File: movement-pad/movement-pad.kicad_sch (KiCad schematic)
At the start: 1 part

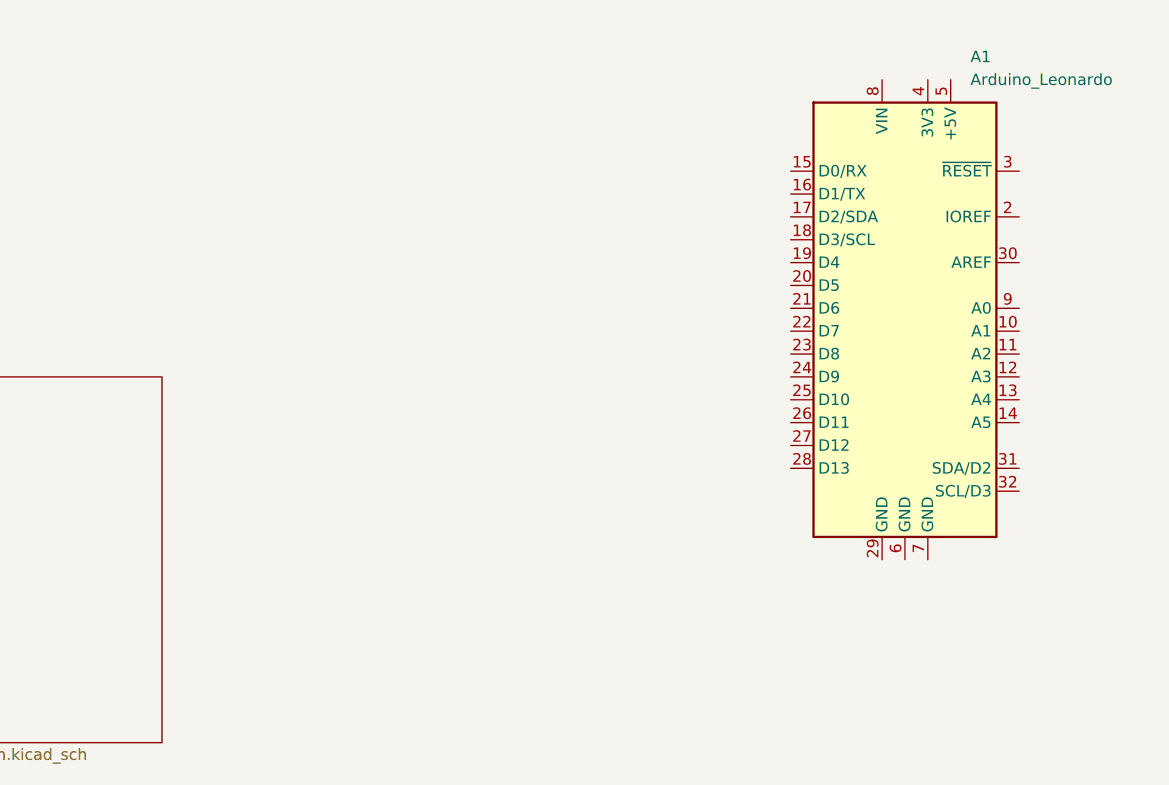
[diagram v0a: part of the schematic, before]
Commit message: worked on schematic in lecture
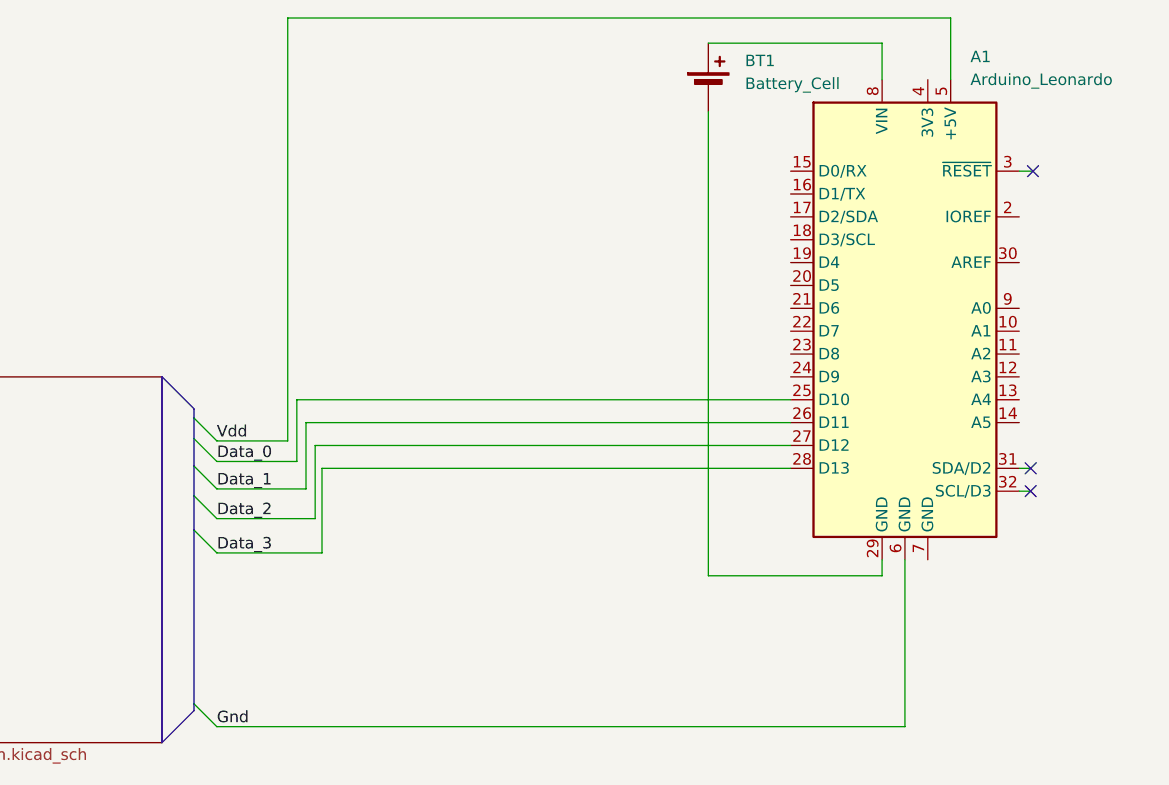
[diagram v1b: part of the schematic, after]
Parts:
- added BT1: Battery_Cell, symbol Device:Battery_Cell
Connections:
- net Data_0: now reaches A1.25 (D10)
- net Data_1: now reaches A1.26 (D11)
- net Data_2: now reaches A1.27 (D12)
- net Data_3: now reaches A1.28 (D13)
- net at A1.29 (GND): now also BT1.2 (-)
- net Vdd: now reaches A1.5 (+5V)
- net Gnd: now reaches A1.6 (GND)
- net at A1.8 (VIN): now also BT1.1 (+)
- no-connect marks 0 -> 3

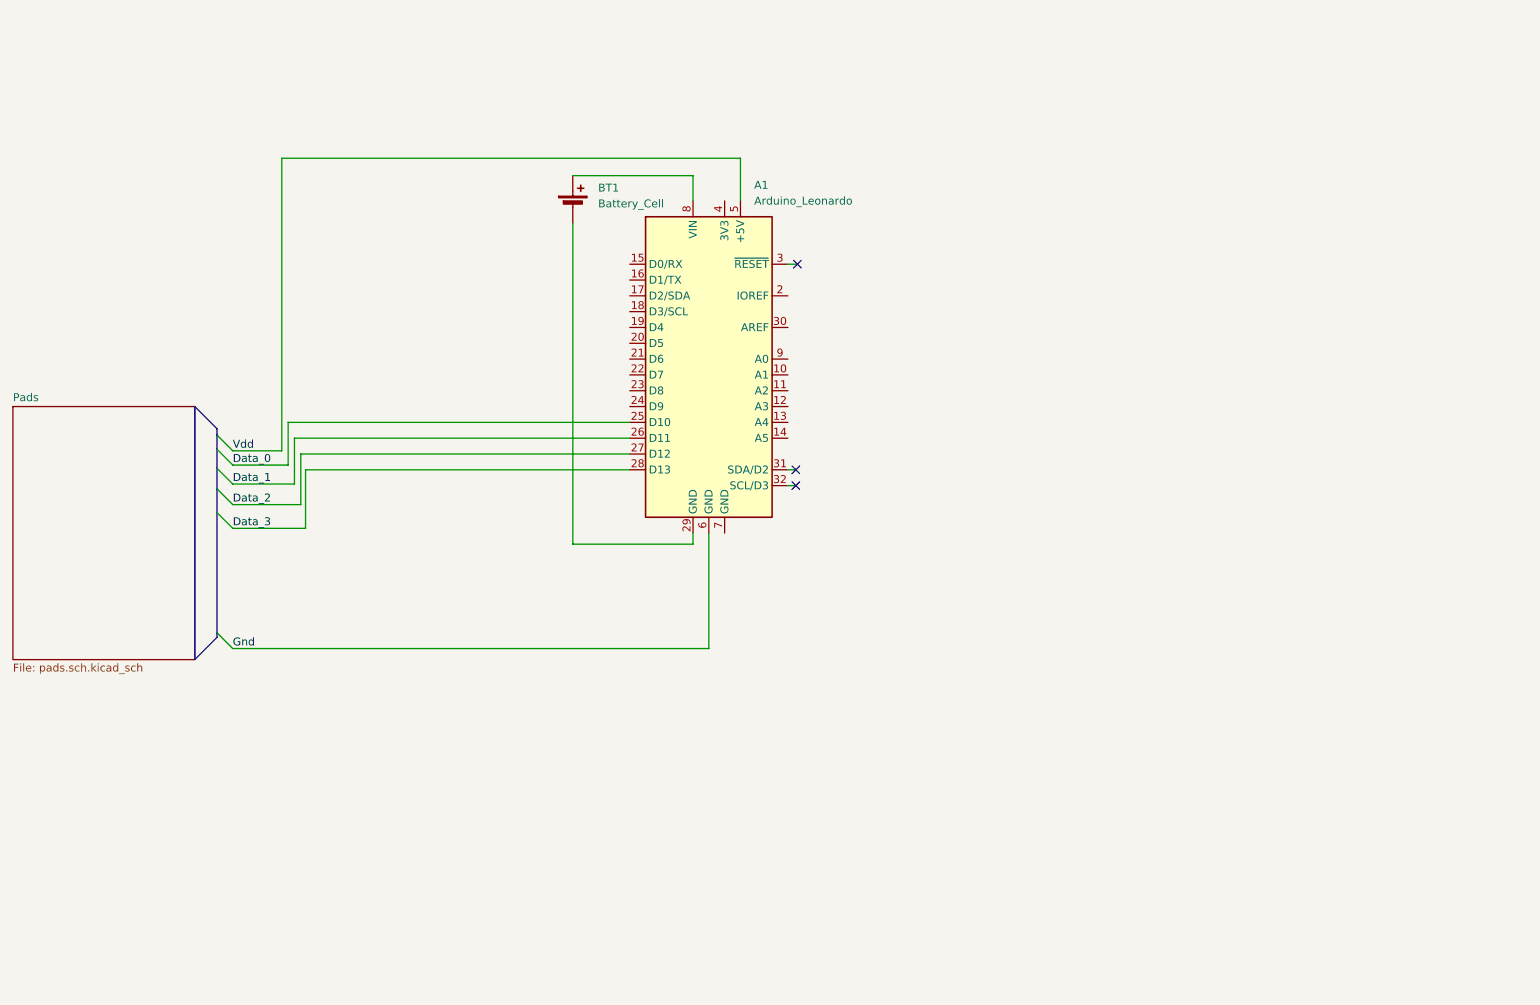
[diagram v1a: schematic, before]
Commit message: updated movement pad
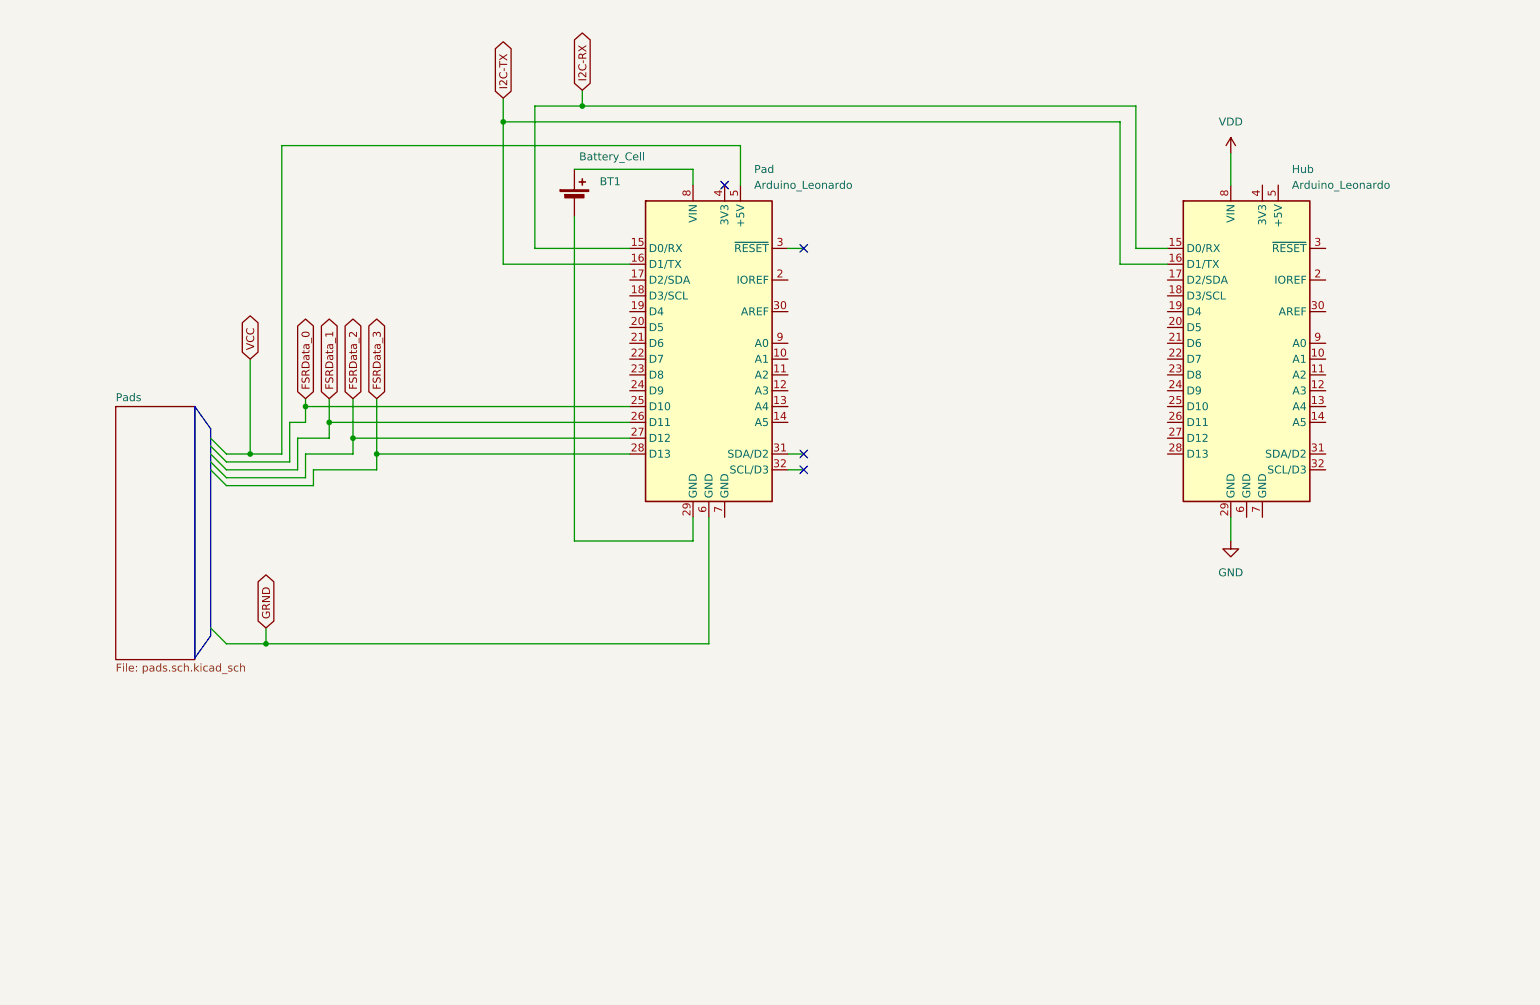
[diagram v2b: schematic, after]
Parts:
- added Hub: Arduino_Leonardo, Module:Arduino_UNO_R3, symbol MCU_Module:Arduino_Leonardo
- renumbered A1 to Pad
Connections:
- net I2C-RX: now reaches Pad.15 (D0/RX)
- net I2C-RX: now also Hub.15 (D0/RX)
- net I2C-TX: now reaches Pad.16 (D1/TX)
- net I2C-TX: now also Hub.16 (D1/TX)
- net Data_0 renamed FSRData_0
- net Data_1 renamed FSRData_1
- net Data_2 renamed FSRData_2
- net Data_3 renamed FSRData_3
- net Gnd renamed GRND
- net Vdd renamed VCC
- new net GND: Hub.29 (GND)
- new net VDD: Hub.8 (VIN)
- no-connect marks 3 -> 4
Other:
- moved on the sheet: BT1, Pad

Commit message: tinkered with top level pad, add in i2c chip?
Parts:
- removed Hub: Arduino_Leonardo, Module:Arduino_UNO_R3, symbol MCU_Module:Arduino_Leonardo
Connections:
- net I2C-RX: no longer names the net of Pad.15 (D0/RX)
- net I2C-TX: no longer names the net of Pad.16 (D1/TX)

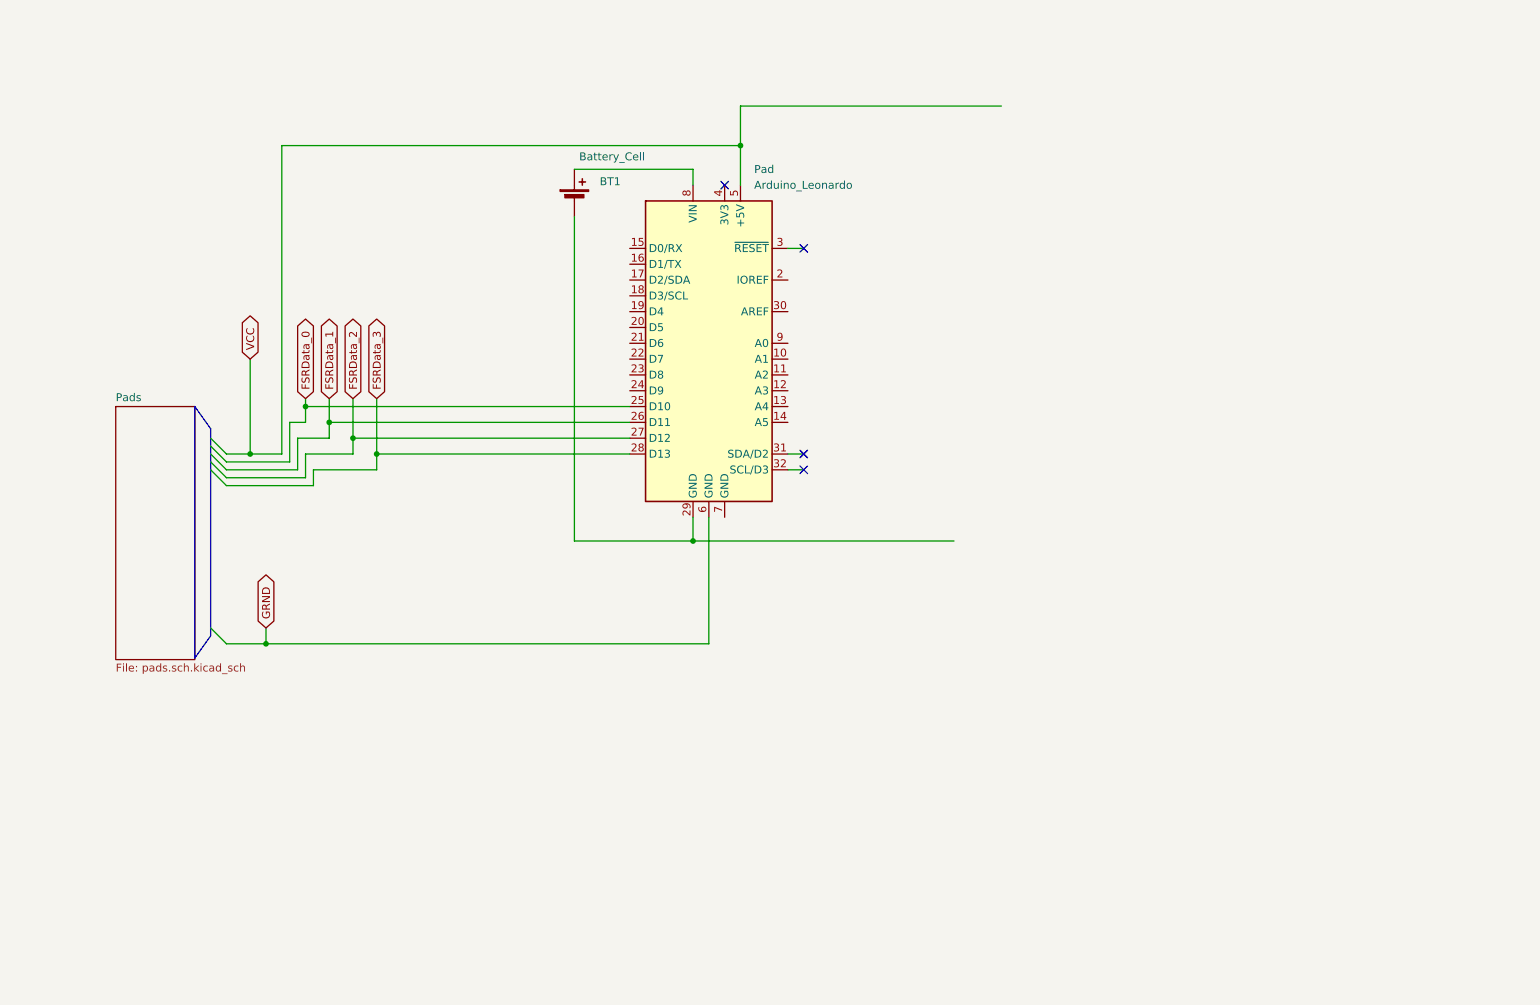
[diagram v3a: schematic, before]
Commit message: added LEDs
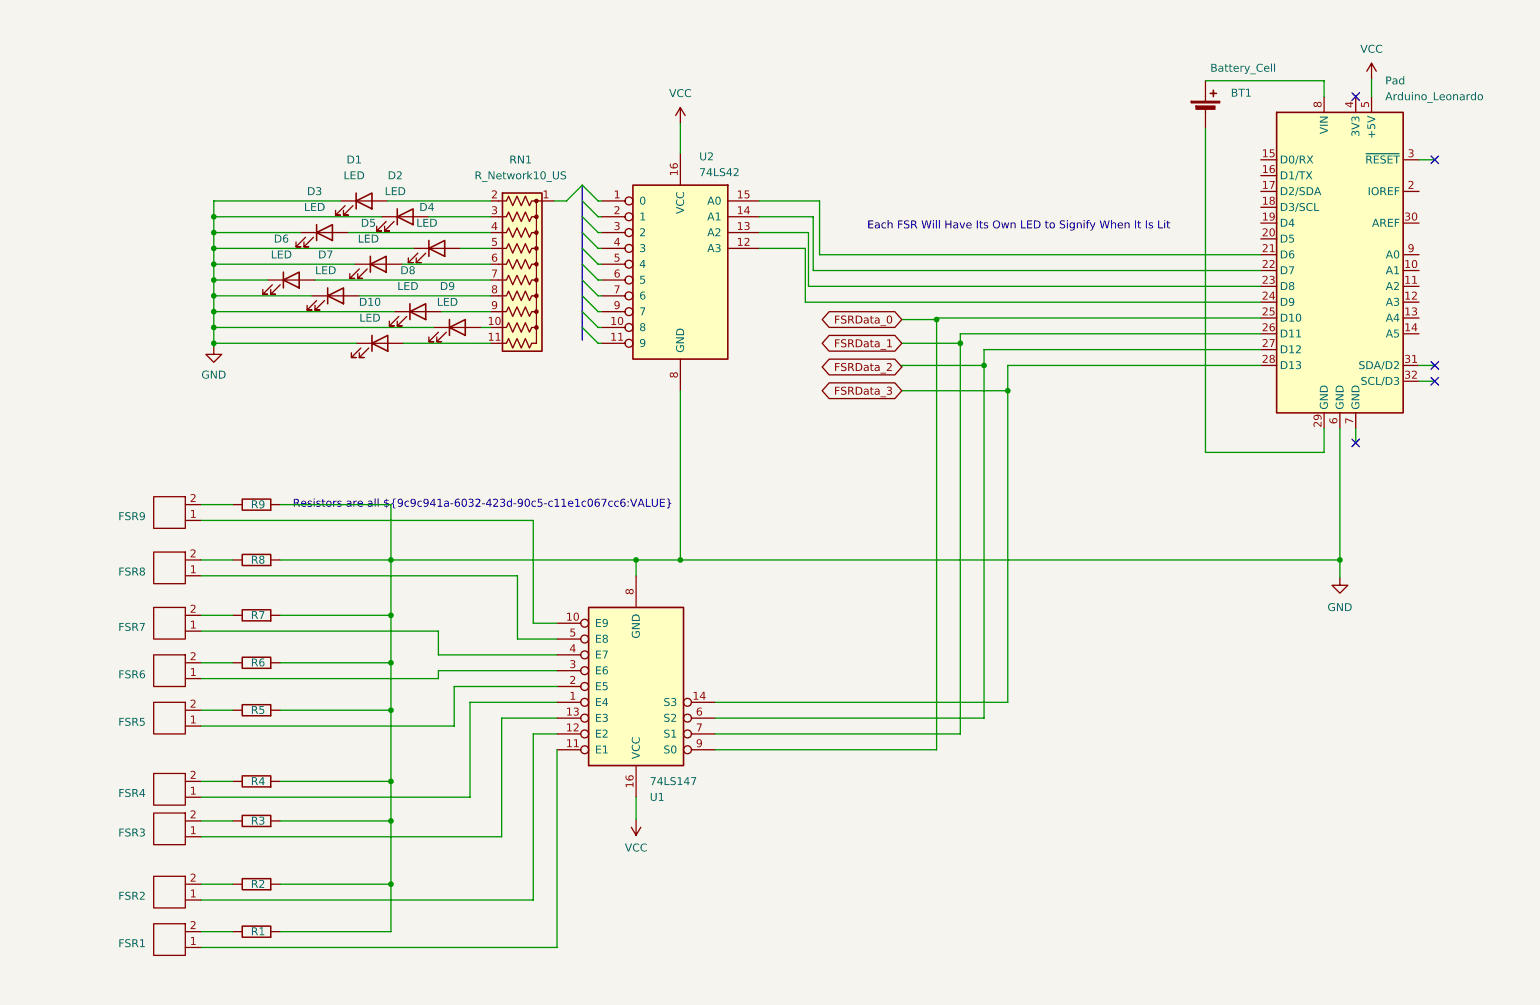
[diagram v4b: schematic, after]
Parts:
- added D1, D10, D2, D3, D4, D5, D6, D7, D8, D9: LED, symbol Device:LED
- added FSR1, FSR2, FSR3, FSR4, FSR5, FSR6, FSR7, FSR8, FSR9: ~, symbol GunProject_lib:FSR
- added R1, R2, R3, R4, R5, R6, R7, R8, R9: 390ohm, Resistor_THT:R_Axial_DIN0207_L6.3mm_D2.5mm_P10.16mm_Horizontal, symbol PCM_SL_Resistors:390ohm
- added RN1: R_Network10_US, Resistor_THT:R_Array_SIP11, symbol Device:R_Network10_US
- added U1: 74LS147, symbol 74xx:74LS147
- added U2: 74LS42, symbol 74xx:74LS42
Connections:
- net FSRData_0: now also U1.9 (S0)
- net FSRData_1: now also U1.7 (S1)
- net FSRData_2: now also U1.6 (S2)
- net FSRData_3: now also U1.14 (S3)
- net VCC: now also U1.16 (VCC), U2.16 (VCC)
- net at Pad.21 (D6): now also U2.15 (A0)
- net at Pad.22 (D7): now also U2.14 (A1)
- net at Pad.23 (D8): now also U2.13 (A2)
- net at Pad.24 (D9): now also U2.12 (A3)
- net GRND renamed GND
- net GND: now also D1.1 (K), D10.1 (K), D2.1 (K), D3.1 (K), D4.1 (K), D5.1 (K), D6.1 (K), D7.1 (K), D8.1 (K), D9.1 (K), R1.1, R2.1, R3.1, R4.1, R5.1, R6.1, R7.1, R8.1, R9.1, U1.8 (GND), U2.8 (GND)
- new net: D9.2 (A), RN1.10 (R9)
- new net: D5.2 (A), RN1.6 (R5)
- new net: D7.2 (A), RN1.8 (R7)
- new net: D2.2 (A), RN1.3 (R2)
- new net: FSR5.2, R5.2
- new net: FSR3.1, U1.13 (E3)
- new net: FSR3.2, R3.2
- new net: FSR7.2, R7.2
- new net: FSR4.1, U1.1 (E4)
- new net: FSR9.1, U1.10 (E9)
- new net: FSR1.1, U1.11 (E1)
- new net: FSR2.1, U1.12 (E2)
- new net: FSR5.1, U1.2 (E5)
- new net: FSR6.1, U1.3 (E6)
- new net: FSR7.1, U1.4 (E7)
- new net: FSR8.1, U1.5 (E8)
- new net: FSR1.2, R1.2
- new net: FSR4.2, R4.2
- new net: D4.2 (A), RN1.5 (R4)
- new net: FSR6.2, R6.2
- new net: FSR2.2, R2.2
- new net: FSR9.2, R9.2
- new net: D10.2 (A), RN1.11 (R10)
- new net: D3.2 (A), RN1.4 (R3)
- new net: D1.2 (A), RN1.2 (R1)
- new net: D6.2 (A), RN1.7 (R6)
- new net: D8.2 (A), RN1.9 (R8)
- new net: FSR8.2, R8.2
- no-connect marks 4 -> 5
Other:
- removed sheet Pads
- note added: "Each FSR Will Have Its Own LED to Signify When It Is Lit"
- note added: "Resistors are all ${9c9c941a-6032-423d-90c5-c11e1c067cc6:VALUE}"
- moved on the sheet: BT1, Pad

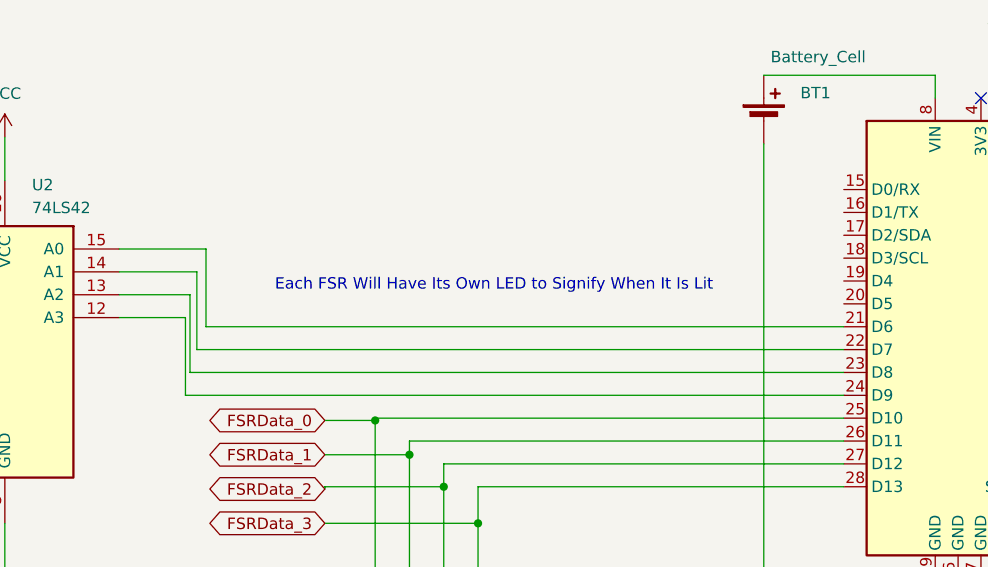
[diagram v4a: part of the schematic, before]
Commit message: Added pad project and edited pad schematic
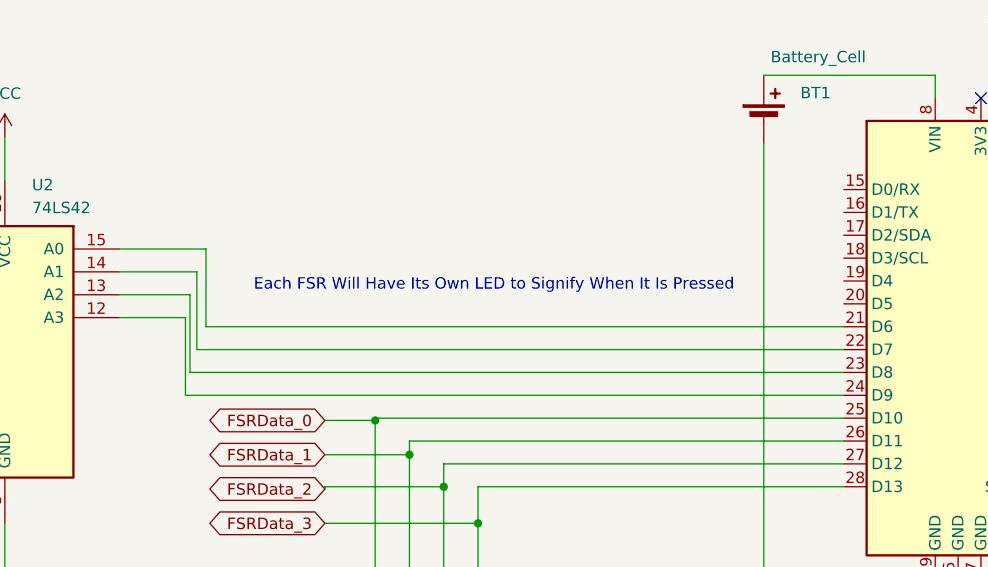
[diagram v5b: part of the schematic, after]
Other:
- note added: "Each FSR Will Have Its Own LED to Signify When It Is Pressed"
- note removed: "Each FSR Will Have Its Own LED to Signify When It Is Lit"
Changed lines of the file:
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@@
 		)
 	)
-	(text "Each FSR Will Have Its Own LED to Signify When It Is Lit"
+	(text "Each FSR Will Have Its Own LED to Signify When It Is Pressed"
 		(exclude_from_sim no)
 		(at 186.944 44.704 0)
